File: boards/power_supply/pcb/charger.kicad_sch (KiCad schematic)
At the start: 42 parts, among them J301 Conn_01x02_Socket, J302 Conn_01x04_Socket

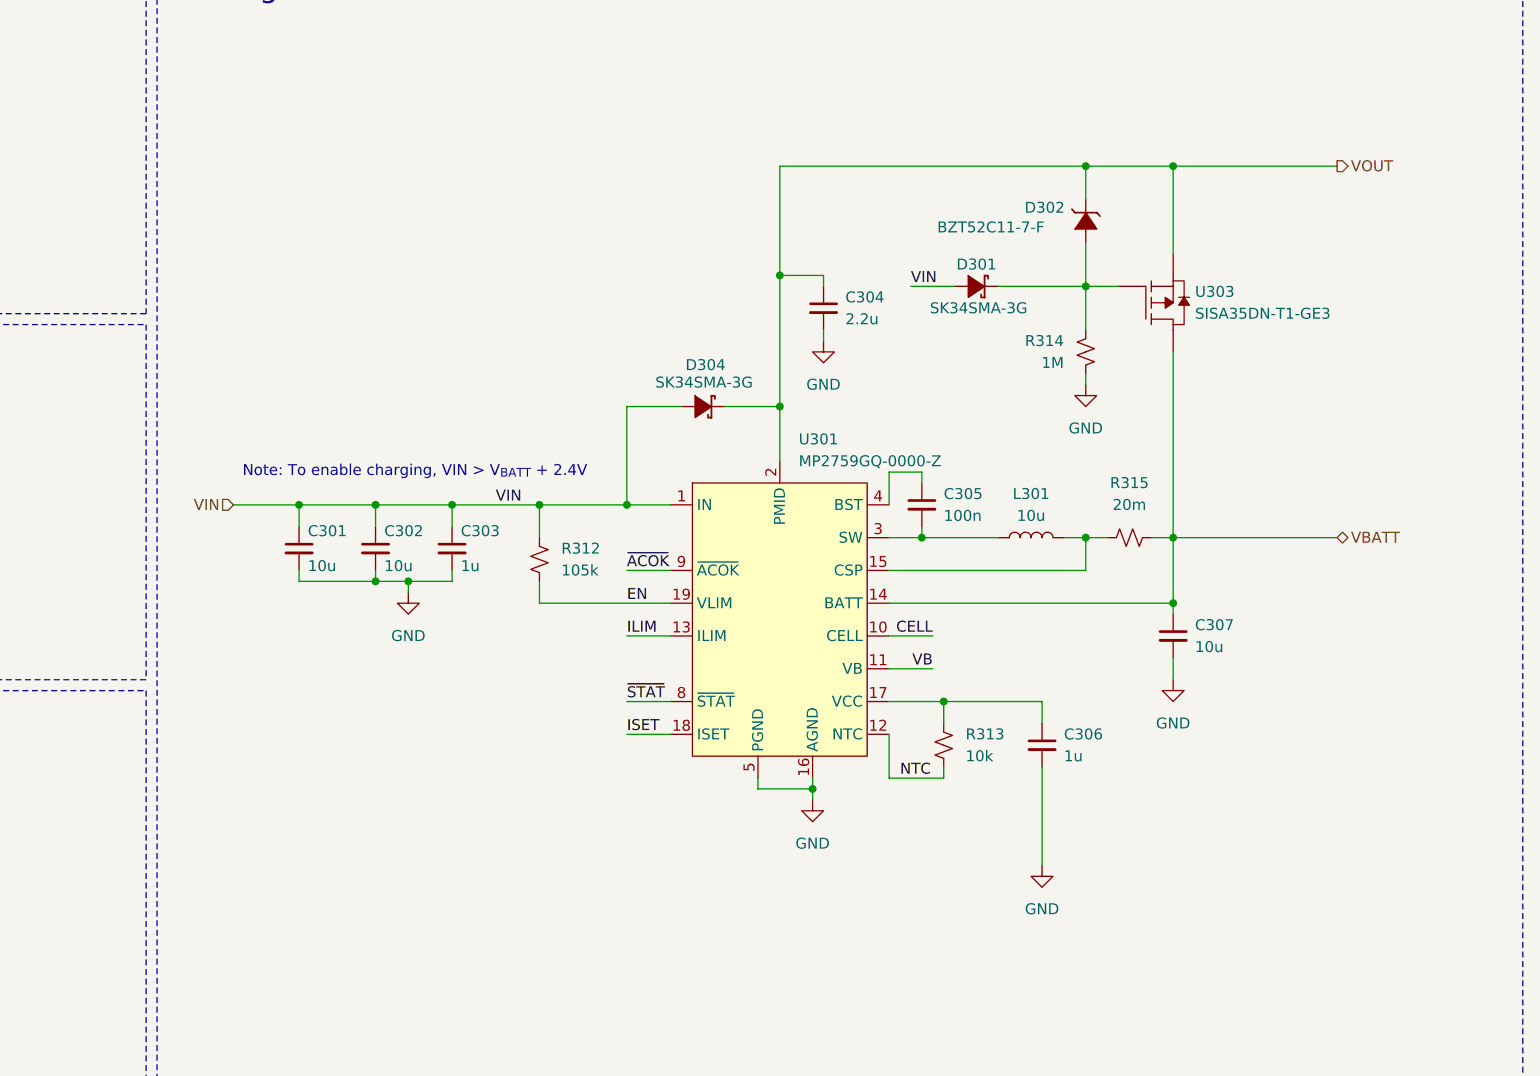
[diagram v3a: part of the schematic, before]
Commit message: created psu footprints
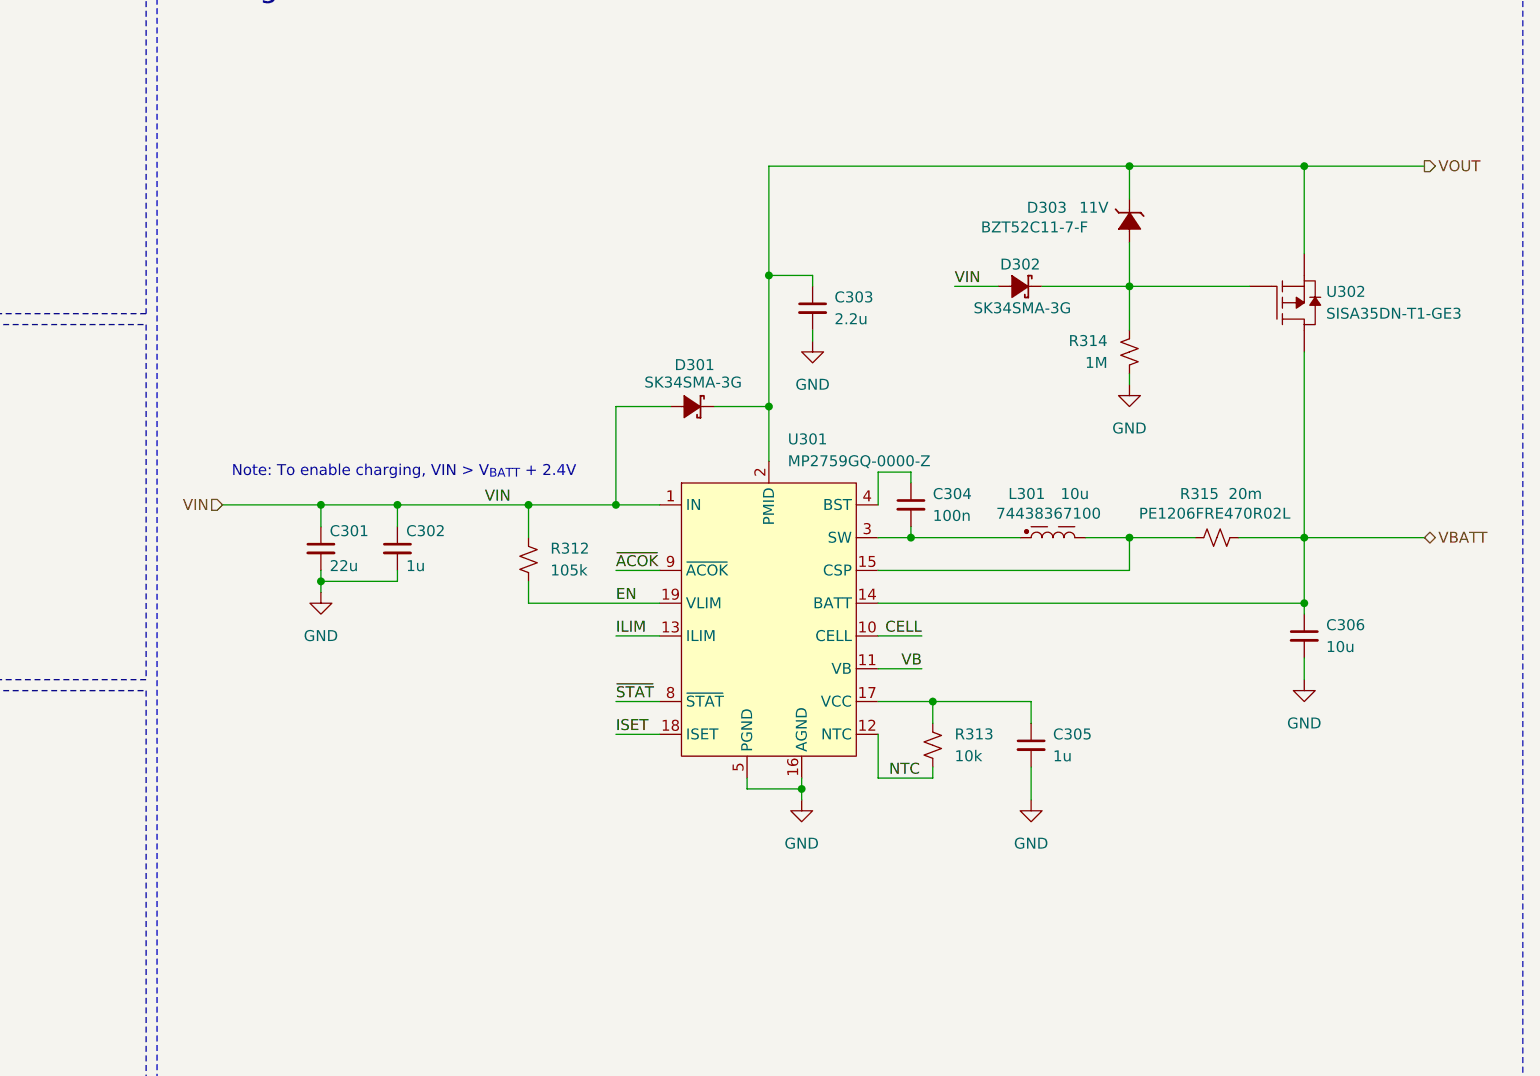
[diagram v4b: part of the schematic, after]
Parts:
- removed C301: 10u, symbol Device:C_Small
- removed L301: 10u, symbol Device:L
- removed R315: 20m, symbol Device:R_Small_US
- added L301: 10u, 74438367100:74438367100, symbol 74438367100:74438367100
- added R315: 20m, PE1206FRE470R02L:PE1206FRE470R02L, symbol PE1206FRE470R02L:PE1206FRE470R02L
- C301: renamed from C302; value 10u -> 22u
- D301: renamed from D304; footprint (none) -> SK34SMA-3G:SK34SMA-3G
- D302: renamed from D301; footprint (none) -> SK34SMA-3G:SK34SMA-3G
- D303: renamed from D302; value ~ -> 11V
- renumbered C303 to C302, C304 to C303, C305 to C304, C306 to C305, C307 to C306, U303 to U302
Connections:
- net VBATT: now also R315.2
- net at U301.15 (CSP): now also L301.2, R315.1
- net at C304.2, U301.3 (SW): now also L301.1
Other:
- moved on the sheet: C301, C302, C303, C304, C305, C306, D301, D302, D303, R312, R313, R314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

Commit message: starting psu layout
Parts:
- C301: footprint (none) -> Capacitor_SMD:C_1206_3216Metric
- C302, C303, C304, C305: footprint (none) -> Capacitor_SMD:C_0603_1608Metric
- C306: footprint (none) -> Capacitor_SMD:C_0805_2012Metric
- D303: footprint (none) -> BZT52C11-7-F:BZT52C11-7-F
- J301: footprint (none) -> Connector_PinHeader_2.54mm:PinHeader_1x02_P2.54mm_Vertical
- J302: footprint (none) -> Connector_PinHeader_2.54mm:PinHeader_1x04_P2.54mm_Vertical
- JP301, JP302, JP303, JP304, JP305, JP306, JP307, JP308, JP309, JP310, JP311, JP312: footprint (none) -> Jumper:SolderJumper-2_P1.3mm_Open_RoundedPad1.0x1.5mm
- R301, R302, R303, R304, R305, R306, R307, R308, R309, R310, R311, R312, R313, R314: footprint (none) -> Resistor_SMD:R_0603_1608Metric
- U301: footprint (none) -> MP2759GQ-0000-Z:MP2759GQ-0000-Z
- U302: footprint (none) -> SISA35DN-T1-GE3:SISA35DN-T1-GE3
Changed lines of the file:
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@@
 			)
 		)
-		(property "Footprint" ""
+		(property "Footprint" "Jumper:SolderJumper-2_P1.3mm_Open_RoundedPad1.0x1.5mm"
 			(at 88.9 83.82 0)
 			(effects
@@
 			)
 		)
-		(property "Footprint" ""
+		(property "Footprint" "Jumper:SolderJumper-2_P1.3mm_Open_RoundedPad1.0x1.5mm"
 			(at 153.67 175.26 0)
 			(effects
@@
 			)
 		)
-		(property "Footprint" ""
+		(property "Footprint" "Connector_PinHeader_2.54mm:PinHeader_1x02_P2.54mm_Vertical"
 			(at 22.86 171.45 0)
 			(effects
@@
 			)
 		)
-		(property "Footprint" ""
+		(property "Footprint" "Resistor_SMD:R_0603_1608Metric"
 			(at 39.37 33.02 0)
 			(effects
@@
 			)
 		)
-		(property "Footprint" ""
+		(property "Footprint" "Jumper:SolderJumper-2_P1.3mm_Open_RoundedPad1.0x1.5mm"
 			(at 87.63 40.64 0)
 			(effects
@@
 			)
 		)
-		(property "Footprint" ""
+		(property "Footprint" "MP2759GQ-0000-Z:MP2759GQ-0000-Z"
 			(at 204.216 74.168 0)
 			(effects
@@
 			)
 		)
-		(property "Footprint" ""
+		(property "Footprint" "Resistor_SMD:R_0603_1608Metric"
 			(at 88.9 76.2 0)
 			(effects
@@
 			)
 		)
-		(property "Footprint" ""
+		(property "Footprint" "Jumper:SolderJumper-2_P1.3mm_Open_RoundedPad1.0x1.5mm"
 			(at 64.77 83.82 0)
 			(effects
@@
 			)
 		)
-		(property "Footprint" ""
+		(property "Footprint" "Resistor_SMD:R_0603_1608Metric"
 			(at 234.95 62.23 0)
 			(effects
@@
 			)
 		)
-		(property "Footprint" ""
+		(property "Footprint" "Resistor_SMD:R_0603_1608Metric"
 			(at 87.63 33.02 0)
 			(effects
@@
 			)
 		)
-		(property "Footprint" ""
+		(property "Footprint" "Jumper:SolderJumper-2_P1.3mm_Open_RoundedPad1.0x1.5mm"
 			(at 134.62 175.26 0)
 			(effects
@@
 			)
 		)
-		(property "Footprint" ""
+		(property "Footprint" "Resistor_SMD:R_0603_1608Metric"
 			(at 88.9 121.92 0)
 			(effects
@@
 			)
 		)
-		(property "Footprint" ""
+		(property "Footprint" "Jumper:SolderJumper-2_P1.3mm_Open_RoundedPad1.0x1.5mm"
 			(at 39.37 40.64 0)
 			(effects
@@
 			)
 		)
-		(property "Footprint" ""
+		(property "Footprint" "Jumper:SolderJumper-2_P1.3mm_Open_RoundedPad1.0x1.5mm"
 			(at 88.9 129.54 0)
 			(effects
@@
 			)
 		)
-		(property "Footprint" ""
+		(property "Footprint" "Resistor_SMD:R_0603_1608Metric"
 			(at 212.09 107.95 0)
 			(effects
@@
 			)
 		)
-		(property "Footprint" ""
+		(property "Footprint" "Resistor_SMD:R_0603_1608Metric"
 			(at 165.1 86.36 0)
 			(effects
@@
 			)
 		)
-		(property "Footprint" ""
+		(property "Footprint" "Capacitor_SMD:C_0805_2012Metric"
 			(at 255.27 95.25 0)
 			(effects
@@
 			)
 		)
-		(property "Footprint" ""
+		(property "Footprint" "Resistor_SMD:R_0603_1608Metric"
 			(at 64.77 121.92 0)
 			(effects
@@
 			)
 		)
-		(property "Footprint" ""
+		(property "Footprint" "Capacitor_SMD:C_0603_1608Metric"
 			(at 223.52 107.95 0)
 			(effects
@@
 			)
 		)
-		(property "Footprint" ""
+		(property "Footprint" "SISA35DN-T1-GE3:SISA35DN-T1-GE3"
 			(at 252.73 50.8 0)
 			(effects
@@
 			)
 		)
-		(property "Footprint" ""
+		(property "Footprint" "Jumper:SolderJumper-2_P1.3mm_Open_RoundedPad1.0x1.5mm"
 			(at 50.8 172.72 0)
 			(effects
@@
 			)
 		)
-		(property "Footprint" ""
+		(property "Footprint" "Resistor_SMD:R_0603_1608Metric"
 			(at 50.8 165.1 0)
 			(effects
@@
 			)
 		)
-		(property "Footprint" ""
+		(property "Footprint" "Resistor_SMD:R_0603_1608Metric"
 			(at 39.37 76.2 0)
 			(effects
@@
 			)
 		)
-		(property "Footprint" ""
+		(property "Footprint" "BZT52C11-7-F:BZT52C11-7-F"
 			(at 231.14 48.26 0)
 			(effects
@@
 			)
 		)
-		(property "Footprint" ""
+		(property "Footprint" "Jumper:SolderJumper-2_P1.3mm_Open_RoundedPad1.0x1.5mm"
 			(at 64.77 129.54 0)
 			(effects
@@
 			)
 		)
-		(property "Footprint" ""
+		(property "Footprint" "Jumper:SolderJumper-2_P1.3mm_Open_RoundedPad1.0x1.5mm"
 			(at 64.77 40.64 0)
 			(effects
@@
 			)
 		)
-		(property "Footprint" ""
+		(property "Footprint" "Connector_PinHeader_2.54mm:PinHeader_1x04_P2.54mm_Vertical"
 			(at 90.17 170.18 0)
 			(effects
@@
 			)
 		)
-		(property "Footprint" ""
+		(property "Footprint" "Capacitor_SMD:C_1206_3216Metric"
 			(at 140.97 85.09 0)
 			(effects
@@
 			)
 		)
-		(property "Footprint" ""
+		(property "Footprint" "Resistor_SMD:R_0603_1608Metric"
 			(at 134.62 167.64 0)
 			(effects
@@
 			)
 		)
-		(property "Footprint" ""
+		(property "Footprint" "Capacitor_SMD:C_0603_1608Metric"
 			(at 209.55 80.01 0)
 			(effects
@@
 			)
 		)
-		(property "Footprint" ""
+		(property "Footprint" "Capacitor_SMD:C_0603_1608Metric"
 			(at 198.12 57.15 0)
 			(effects
@@
 			)
 		)
-		(property "Footprint" ""
+		(property "Footprint" "Resistor_SMD:R_0603_1608Metric"
 			(at 153.67 167.64 0)
 			(effects
@@
 			)
 		)
-		(property "Footprint" ""
+		(property "Footprint" "Resistor_SMD:R_0603_1608Metric"
 			(at 64.77 76.2 0)
 			(effects
@@
 			)
 		)
-		(property "Footprint" ""
+		(property "Footprint" "Jumper:SolderJumper-2_P1.3mm_Open_RoundedPad1.0x1.5mm"
 			(at 39.37 83.82 0)
 			(effects
@@
 			)
 		)
-		(property "Footprint" ""
+		(property "Footprint" "Capacitor_SMD:C_0603_1608Metric"
 			(at 149.86 85.09 0)
 			(effects
@@
 			)
 		)
-		(property "Footprint" ""
+		(property "Footprint" "Jumper:SolderJumper-2_P1.3mm_Open_RoundedPad1.0x1.5mm"
 			(at 39.37 129.54 0)
 			(effects
@@
 			)
 		)
-		(property "Footprint" ""
+		(property "Footprint" "Resistor_SMD:R_0603_1608Metric"
 			(at 64.77 33.02 0)
 			(effects

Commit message: initial psu charger layout
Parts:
- J301: footprint Connector_PinHeader_2.54mm:PinHeader_1x02_P2.54mm_Vertical -> Connector_JST:JST_XH_B2B-XH-A_1x02_P2.50mm_Vertical
- J302: footprint Connector_PinHeader_2.54mm:PinHeader_1x04_P2.54mm_Vertical -> Connector_JST:JST_XH_B4B-XH-A_1x04_P2.50mm_Vertical
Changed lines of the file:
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@@
 		)
 	)
-	(label "ILIM"
-		(at 39.37 29.21 0)
+	(label "VBATT"
+		(at 260.35 83.82 0)
 		(fields_autoplaced yes)
 		(effects
@@
 		)
 	)
-	(label "NTC"
-		(at 50.8 161.29 0)
+	(label "ILIM"
+		(at 39.37 29.21 0)
 		(fields_autoplaced yes)
 		(effects
@@
 		)
 	)
-	(label "~{STAT}"
-		(at 101.6 170.18 180)
+	(label "VOUT"
+		(at 260.35 40.64 0)
 		(fields_autoplaced yes)
 		(effects
@@
 				(size 1.27 1.27)
 			)
-			(justify right bottom)
-		)
-	)
-	(label "ISET"
-		(at 39.37 72.39 0)
+			(justify left bottom)
+		)
+	)
+	(label "NTC"
+		(at 50.8 161.29 0)
 		(fields_autoplaced yes)
 		(effects
@@
 		)
 	)
-	(label "ISET"
-		(at 175.26 106.68 0)
+	(label "~{STAT}"
+		(at 101.6 170.18 180)
 		(fields_autoplaced yes)
 		(effects
@@
 				(size 1.27 1.27)
 			)
-			(justify left bottom)
-		)
-	)
-	(label "ILIM"
-		(at 175.26 95.25 0)
+			(justify right bottom)
+		)
+	)
+	(label "ISET"
+		(at 39.37 72.39 0)
 		(fields_autoplaced yes)
 		(effects
@@
 		)
 	)
+	(label "ISET"
+		(at 175.26 106.68 0)
+		(fields_autoplaced yes)
+		(effects
+			(font
+				(size 1.27 1.27)
+			)
+			(justify left bottom)
+		)
+	)
+	(label "ILIM"
+		(at 175.26 95.25 0)
+		(fields_autoplaced yes)
+		(effects
+			(font
+				(size 1.27 1.27)
+			)
+			(justify left bottom)
+		)
+	)
 	(hierarchical_label "VBATT"
 		(shape bidirectional)
@@
 			)
 		)
-		(property "Footprint" "Connector_PinHeader_2.54mm:PinHeader_1x02_P2.54mm_Vertical"
+		(property "Footprint" "Connector_JST:JST_XH_B2B-XH-A_1x02_P2.50mm_Vertical"
 			(at 22.86 171.45 0)
 			(effects
@@
 			)
 		)
-		(property "Footprint" "Connector_PinHeader_2.54mm:PinHeader_1x04_P2.54mm_Vertical"
+		(property "Footprint" "Connector_JST:JST_XH_B4B-XH-A_1x04_P2.50mm_Vertical"
 			(at 90.17 170.18 0)
 			(effects

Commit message: psu layouting
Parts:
- C303: footprint Capacitor_SMD:C_0603_1608Metric -> Capacitor_SMD:C_1206_3216Metric
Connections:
- net VBATT: no longer U302.6, U302.7, U302.8
- net VOUT: no longer U302.2, U302.3
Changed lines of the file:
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@@
 		(on_board yes)
 		(dnp no)
-		(fields_autoplaced yes)
 		(property "Reference" "U301"
 			(at 195.2341 72.39 0)
@@
 			)
 		)
-		(pin "2"
-		)
-		(pin "3"
-		)
-		(pin "7"
-		)
-		(pin "6"
-		)
 		(pin "4"
-		)
-		(pin "8"
 		)
 		(pin "1"
@@
 			)
 		)
-		(property "Footprint" "Capacitor_SMD:C_0603_1608Metric"
+		(property "Footprint" "Capacitor_SMD:C_1206_3216Metric"
 			(at 198.12 57.15 0)
 			(effects
